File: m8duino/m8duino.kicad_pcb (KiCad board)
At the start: 2 copper layers, 76.2 x 50.8 mm, 18 parts, among them J1 Conn_02x03_Odd_Even, J2 Conn_01x02, J3 Conn_01x02, J4 Conn_01x02, J5 Conn_01x02, J6 Conn_01x02, SW1 SW_Push_LED, SW2 SW_Push_LED, SW3 SW_Push_LED, U1 ATMEGA8-16PU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

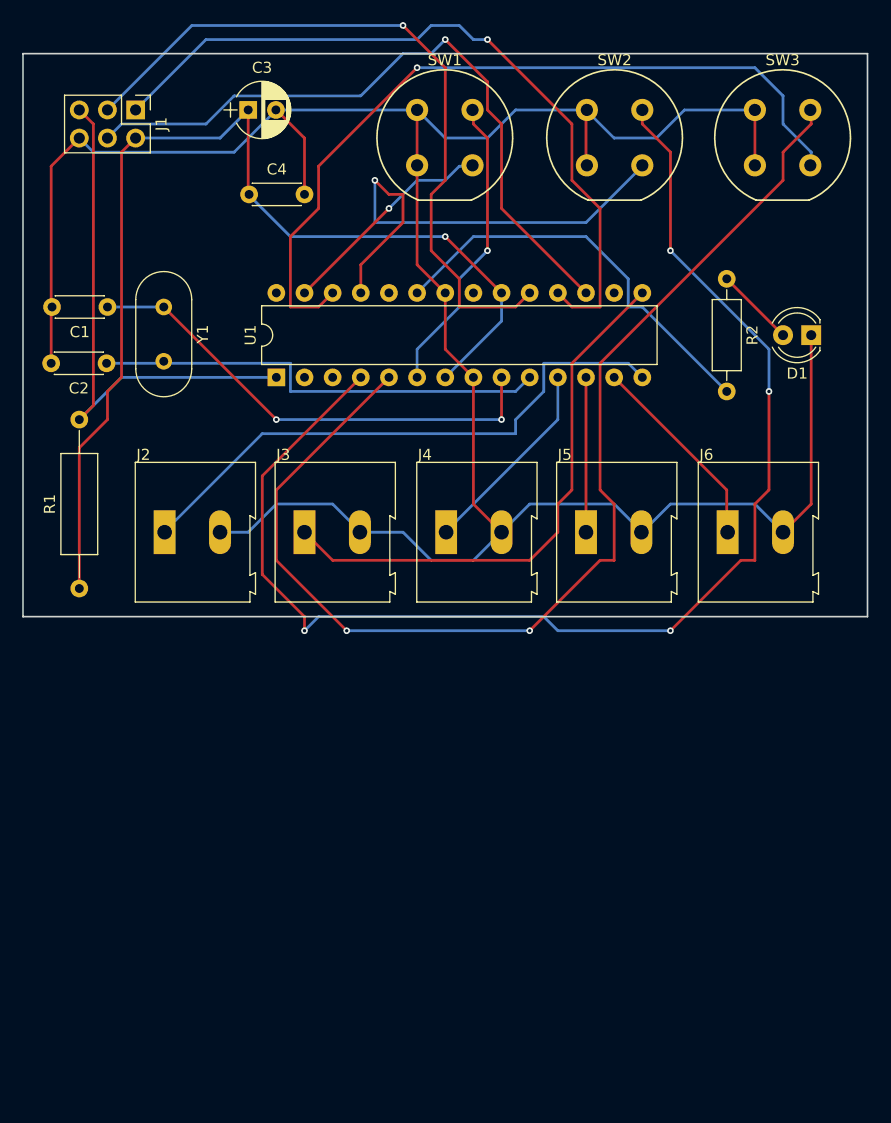
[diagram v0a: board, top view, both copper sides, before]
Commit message: 调整为 Arduino 系统开发板
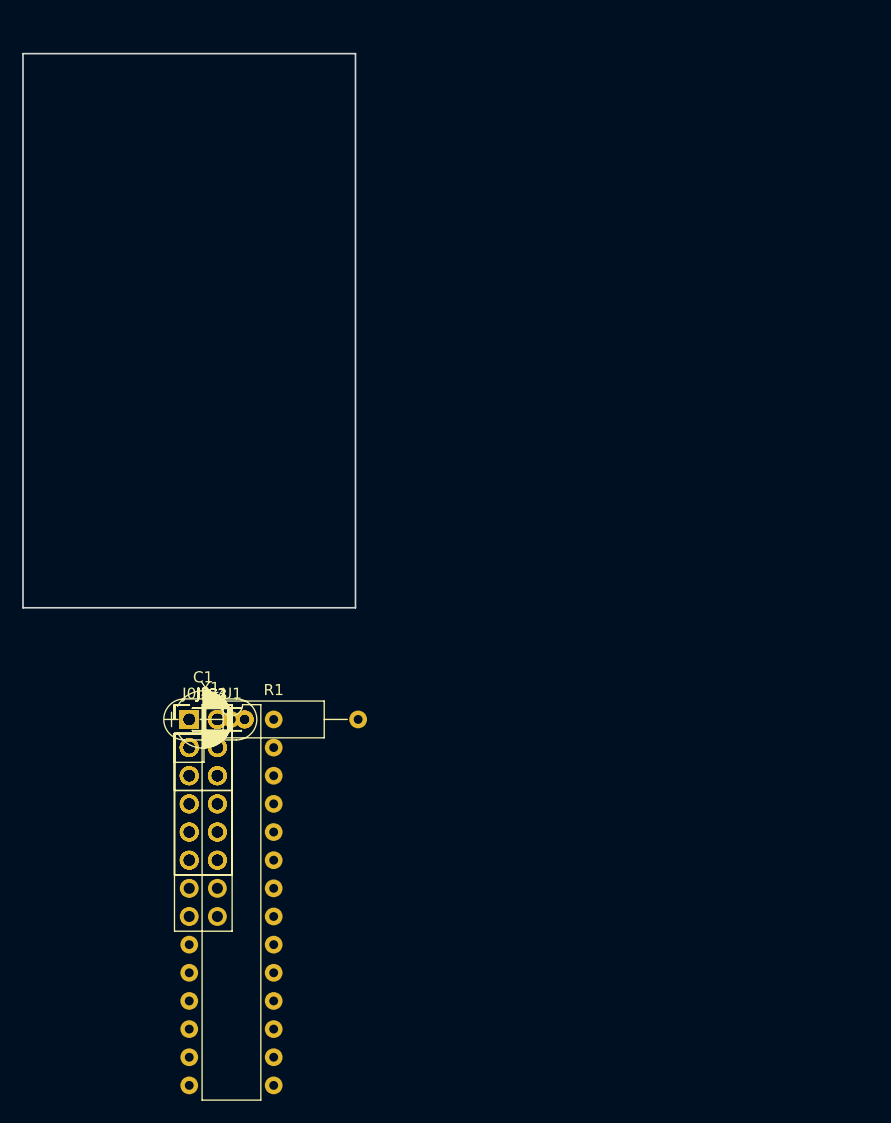
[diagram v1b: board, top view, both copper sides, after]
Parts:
- removed D1: LED, LEDs:LED_D4.0mm
- removed J6: Conn_01x02, Connectors_Terminal_Blocks:TerminalBlock_Altech_AK300-2_P5.00mm
- removed R2: R, Resistors_THT:R_Axial_DIN0207_L6.3mm_D2.5mm_P10.16mm_Horizontal
- removed SW1, SW2, SW3: SW_Push_LED, Buttons_Switches_THT:Push_E-Switch_KS01Q01
- added J0: Conn_01x02, Pin_Headers:Pin_Header_Straight_1x02_Pitch2.54mm, F.Cu at (152.2, 156.6)
- C1: value 22pF -> 10uF; footprint Capacitors_THT:C_Disc_D4.3mm_W1.9mm_P5.00mm -> Capacitors_THT:CP_Radial_D5.0mm_P2.50mm
- C2: value 22pF -> 10pF
- C3: value 10uF -> 22pF; footprint Capacitors_THT:CP_Radial_D5.0mm_P2.50mm -> Capacitors_THT:C_Disc_D4.3mm_W1.9mm_P5.00mm
- C4: value 10pF -> 22pF
- J1: value Conn_02x03_Odd_Even -> ISP
- J2: value Conn_01x02 -> ANA; footprint Connectors_Terminal_Blocks:TerminalBlock_Altech_AK300-2_P5.00mm -> Pin_Headers:Pin_Header_Straight_2x03_Pitch2.54mm
- J3: value Conn_01x02 -> D8-13; footprint Connectors_Terminal_Blocks:TerminalBlock_Altech_AK300-2_P5.00mm -> Pin_Headers:Pin_Header_Straight_2x06_Pitch2.54mm
- J4: value Conn_01x02 -> A0-5; footprint Connectors_Terminal_Blocks:TerminalBlock_Altech_AK300-2_P5.00mm -> Pin_Headers:Pin_Header_Straight_2x06_Pitch2.54mm
- J5: value Conn_01x02 -> D0-7; footprint Connectors_Terminal_Blocks:TerminalBlock_Altech_AK300-2_P5.00mm -> Pin_Headers:Pin_Header_Straight_2x08_Pitch2.54mm
- U1: value ATMEGA8-16PU -> ATMEGA8L-8PU
- Y1: footprint Crystals:Crystal_HC18-U_Vertical -> Crystals:Crystal_HC52-U_Vertical
- moved C3 55.3 mm to (152.2, 156.6)
- moved J1 55.2 mm to (152.2, 156.6), turned to 0 degrees
- moved C4 47.7 mm to (152.2, 156.6)
- moved J5 39.6 mm to (152.2, 156.6)
- moved C1 37.9 mm to (152.2, 156.6), turned to 0 degrees
- moved Y1 37.3 mm to (152.2, 156.6), turned to 0 degrees
- moved C2 33.0 mm to (152.2, 156.6), turned to 0 degrees
- moved U1 31.9 mm to (152.2, 156.6), turned to 0 degrees
- moved J4 28.7 mm to (152.2, 156.6)
- moved J3 19.8 mm to (152.2, 156.6)
- moved J2 17.0 mm to (152.2, 156.6)
- moved R1 15.4 mm to (152.2, 156.6), turned to 0 degrees
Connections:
- C1 pad 1: Net-(C1-Pad1) -> +5V
- C2 pad 1: Net-(C2-Pad1) -> +5V
- C3 pad 1: +5V -> Net-(C3-Pad1)
- C4 pad 1: +5V -> Net-(C4-Pad1)
- J2 pad 1: /D8 -> (no net)
- J2 pad 2: GND -> (no net)
- J3 pad 1: /D9 -> (no net)
- J3 pad 2: GND -> (no net)
- J4 pad 1: /D5 -> (no net)
- J4 pad 2: GND -> (no net)
- J5 pad 1: /D6 -> (no net)
- J5 pad 2: GND -> (no net)
- U1 pad 10: Net-(C2-Pad1) -> Net-(C4-Pad1)
- U1 pad 11: /D5 -> (no net)
- U1 pad 12: /D6 -> (no net)
- U1 pad 13: /D7 -> (no net)
- U1 pad 14: /D8 -> (no net)
- U1 pad 15: /D9 -> (no net)
- U1 pad 16: /D10 -> (no net)
- U1 pad 2: /D0 -> (no net)
- U1 pad 20: +5V -> (no net)
- U1 pad 21: Net-(U1-Pad21) -> (no net)
- U1 pad 22: GND -> (no net)
- U1 pad 23: /A0 -> (no net)
- U1 pad 24: /A1 -> (no net)
- U1 pad 25: /A2 -> (no net)
- U1 pad 26: /A3 -> (no net)
- U1 pad 27: /A4 -> (no net)
- U1 pad 28: /A5 -> (no net)
- U1 pad 3: /D1 -> (no net)
- U1 pad 4: /BTN_WORK_A -> (no net)
- U1 pad 5: /BTN_WORK_M -> (no net)
- U1 pad 6: /BTN_WASH -> (no net)
- U1 pad 9: Net-(C1-Pad1) -> Net-(C3-Pad1)
- Y1 pad 1: Net-(C1-Pad1) -> Net-(C4-Pad1)
- Y1 pad 2: Net-(C2-Pad1) -> Net-(C3-Pad1)
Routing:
- net GND: track 227.7 -> 0.00 mm
- net /BTN_WORK_A: track 118.3 -> 0.00 mm, vias 4 -> 0
- net /BTN_WORK_M: track 105.6 -> 0.00 mm, vias 2 -> 0
- net +5V: track 98.0 -> 0.00 mm, vias 1 -> 0
- net /A3: track 72.2 -> 0.00 mm, vias 1 -> 0
- net /D12: track 68.1 -> 0.00 mm, vias 1 -> 0
- net /D13: track 65.3 -> 0.00 mm, vias 1 -> 0
- net /D11: track 62.3 -> 0.00 mm, vias 1 -> 0
- net /D8: track 52.3 -> 0.00 mm
- net /D9: track 49.7 -> 0.00 mm
- net /RESET: track 48.4 -> 0.00 mm
- net /A2: track 43.7 -> 0.00 mm, vias 1 -> 0
- net Net-(C1-Pad1): track 43.6 -> 0.00 mm, vias 2 -> 0
- net Net-(C2-Pad1): track 41.6 -> 0.00 mm
- net /A0: track 37.3 -> 0.00 mm
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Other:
- board size 76.2 x 50.8 mm -> 30 x 50 mm
